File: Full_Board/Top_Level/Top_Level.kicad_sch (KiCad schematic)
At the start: 7 parts, among them J1 OQ0212500000G, J2 OQ0212500000G, J3 OQ0432500000G, J4 OQ0432500000G, J5 OQ0432500000G

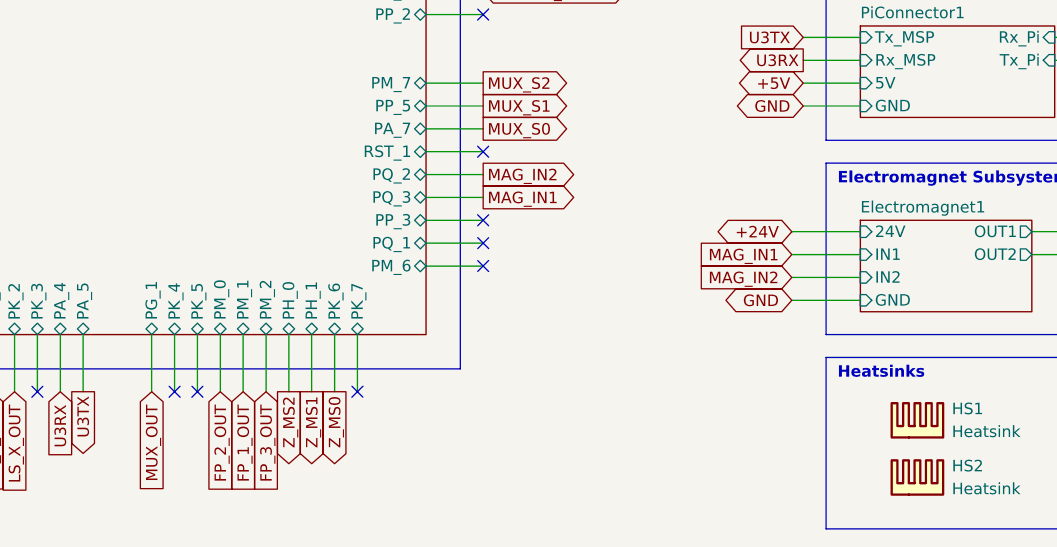
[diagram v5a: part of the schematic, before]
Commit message: Added traces for emag and increased the width of some power lines
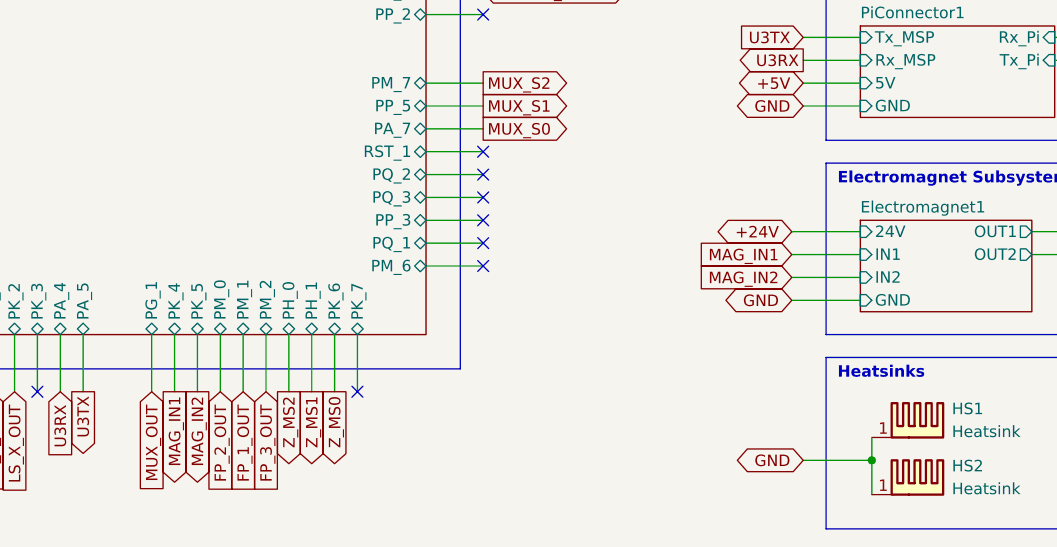
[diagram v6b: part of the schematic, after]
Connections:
- net GND: now also HS1.1, HS2.1
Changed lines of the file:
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@@
     (company "The Great Gambit")
   )
+  (junction (at 151.13 185.42) (diameter 0) (color 0 0 0 0)
+  )
   (no_connect (at 81.28 96.52))
   (no_connect (at 78.74 96.52))
@@
   (no_connect (at 40.64 96.52))
   (no_connect (at 107.95 135.89))
+  (no_connect (at 107.95 153.67))
+  (no_connect (at 107.95 156.21))
   (no_connect (at 107.95 158.75))
   (no_connect (at 107.95 120.65))
@@
   (no_connect (at 107.95 161.29))
   (no_connect (at 71.12 96.52))
-  (no_connect (at 73.66 177.8))
-  (no_connect (at 76.2 177.8))
   (no_connect (at 25.4 153.67))
   (no_connect (at 25.4 151.13))
@@
     (stroke (width 0) (type default) (color 0 0 0 0))
   )
+  (wire (pts (xy 101.6 153.67) (xy 107.95 153.67))
+    (stroke (width 0) (type default) (color 0 0 0 0))
+  )
   (wire (pts (xy 25.4 135.89) (xy 31.75 135.89))
     (stroke (width 0) (type default) (color 0 0 0 0))
   )
+  (wire (pts (xy 151.13 185.42) (xy 151.13 189.23))
+    (stroke (width 0) (type default) (color 0 0 0 0))
+  )
   (wire (pts (xy 101.6 151.13) (xy 107.95 151.13))
     (stroke (width 0) (type default) (color 0 0 0 0))
@@
     (stroke (width 0) (type default) (color 0 0 0 0))
   )
+  (wire (pts (xy 143.51 185.42) (xy 151.13 185.42))
+    (stroke (width 0) (type default) (color 0 0 0 0))
+  )
   (wire (pts (xy 223.52 36.83) (xy 228.6 36.83))
     (stroke (width 0) (type default) (color 0 0 0 0))
@@
     (stroke (width 0) (type default) (color 0 0 0 0))
   )
-  (polyline (pts (xy 226.06 154.94) (xy 226.06 119.38))
+  (wire (pts (xy 101.6 156.21) (xy 107.95 156.21))
     (stroke (width 0) (type default) (color 0 0 0 0))
   )
-  (wire (pts (xy 101.6 153.67) (xy 107.95 153.67))
+  (polyline (pts (xy 226.06 154.94) (xy 226.06 119.38))
     (stroke (width 0) (type default) (color 0 0 0 0))
   )
@@
     (stroke (width 0) (type default) (color 0 0 0 0))
   )
+  (wire (pts (xy 151.13 185.42) (xy 151.13 182.88))
+    (stroke (width 0) (type default) (color 0 0 0 0))
+  )
   (polyline (pts (xy 76.2 13.97) (xy 104.14 13.97))
     (stroke (width 0) (type default) (color 0 0 0 0))
@@
     (stroke (width 0) (type default) (color 0 0 0 0))
   )
-  (wire (pts (xy 101.6 156.21) (xy 107.95 156.21))
-    (stroke (width 0) (type default) (color 0 0 0 0))
-  )
   (wire (pts (xy 251.46 24.13) (xy 256.54 24.13))
     (stroke (width 0) (type default) (color 0 0 0 0))
@@
     )
   )
-  (global_label "MAG_IN2" (shape output) (at 107.95 153.67 0) (fields_autoplaced)
-    (effects (font (size 1.27 1.27)) (justify left))
-    (property "Intersheet References" "${INTERSHEET_REFS}" (id 0) (at 118.2855 153.7494 0)
-      (effects (font (size 1.27 1.27)) (justify left) hide)
+  (global_label "MAG_IN2" (shape output) (at 76.2 177.8 270) (fields_autoplaced)
+    (effects (font (size 1.27 1.27)) (justify right))
+    (property "Intersheet References" "${INTERSHEET_REFS}" (id 0) (at 76.1206 188.1355 90)
+      (effects (font (size 1.27 1.27)) (justify right) hide)
     )
   )
@@
     )
   )
-  (global_label "MAG_IN1" (shape output) (at 107.95 156.21 0) (fields_autoplaced)
-    (effects (font (size 1.27 1.27)) (justify left))
-    (property "Intersheet References" "${INTERSHEET_REFS}" (id 0) (at 118.2855 156.2894 0)
-      (effects (font (size 1.27 1.27)) (justify left) hide)
+  (global_label "MAG_IN1" (shape output) (at 73.66 177.8 270) (fields_autoplaced)
+    (effects (font (size 1.27 1.27)) (justify right))
+    (property "Intersheet References" "${INTERSHEET_REFS}" (id 0) (at 73.5806 188.1355 90)
+      (effects (font (size 1.27 1.27)) (justify right) hide)
     )
   )
@@
     )
   )
+  (global_label "GND" (shape bidirectional) (at 143.51 185.42 180) (fields_autoplaced)
+    (effects (font (size 1.27 1.27)) (justify right))
+    (property "Intersheet References" "${INTERSHEET_REFS}" (id 0) (at 137.2264 185.4994 0)
+      (effects (font (size 1.27 1.27)) (justify right) hide)
+    )
+  )
   (global_label "GND" (shape bidirectional) (at 143.51 146.05 180) (fields_autoplaced)
     (effects (font (size 1.27 1.27)) (justify right))
@@
       (effects (font (size 1.27 1.27)) hide)
     )
+    (pin "1")
   )
   (symbol (lib_id "OQ04325500000G:OQ0432500000G") (at 254 99.06 0) (unit 1)
@@
     (pin "2")
   )
-  (symbol (lib_id "Mechanical:Heatsink") (at 156.21 182.88 0) (unit 1)
+  (symbol (lib_name "Heatsink_1") (lib_id "Mechanical:Heatsink") (at 156.21 182.88 0) (unit 1)
     (in_bom yes) (on_board yes) (fields_autoplaced)
     (property "Reference" "HS1" (id 0) (at 160.02 179.7049 0)
@@
       (effects (font (size 1.27 1.27)) hide)
     )
+    (pin "1")
   )
   (symbol (lib_id "OQ04325500000G:OQ0432500000G") (at 254 67.31 0) (unit 1)
@@
       (reference "TP15") (unit 1) (value "~") (footprint "TestPoint:TestPoint_Keystone_5010-5014_Multipurpose")
     )
+    (path "/f059198e-ec55-48b1-bb71-d05bde55edab/63ce05dd-a994-434a-9d25-50da649a6ec3"
+      (reference "TP16") (unit 1) (value "~") (footprint "TestPoint:TestPoint_Keystone_5010-5014_Multipurpose")
+    )
+    (path "/f059198e-ec55-48b1-bb71-d05bde55edab/d8216112-e73b-4580-b202-27b92baacd12"
+      (reference "TP17") (unit 1) (value "~") (footprint "TestPoint:TestPoint_Keystone_5010-5014_Multipurpose")
+    )
     (path "/f355d1b6-bee3-4968-acb9-caad2ec6238b/51b51704-6420-43a3-8572-c2e2ef1291bf"

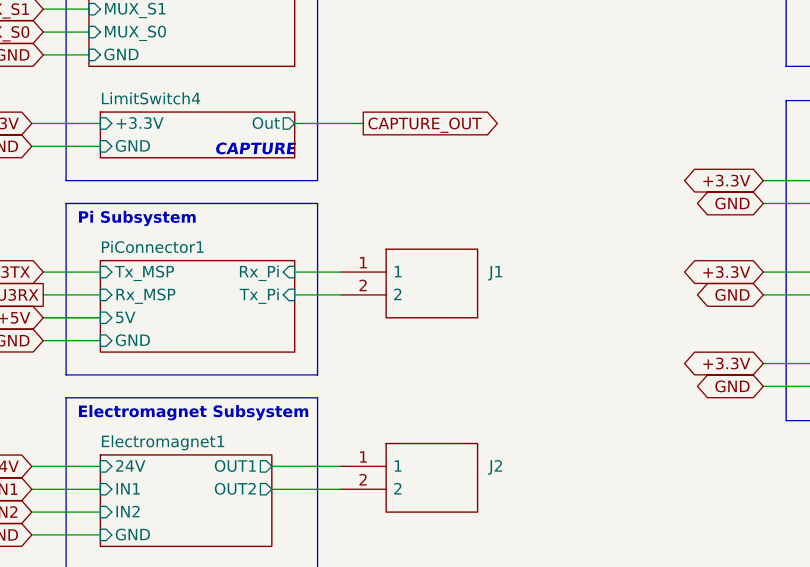
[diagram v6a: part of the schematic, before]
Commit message: Added Pi header
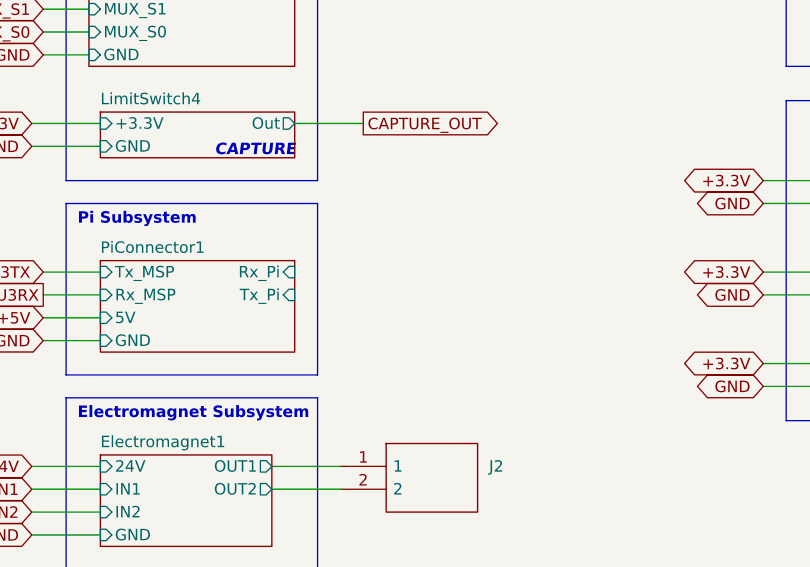
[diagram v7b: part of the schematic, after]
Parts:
- removed J1: OQ0212500000G, OQ0212500000G:OQ0212500000G, symbol OQ0212500000G:OQ0212500000G
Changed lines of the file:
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@@
     (stroke (width 0) (type default) (color 0 0 0 0))
   )
-  (wire (pts (xy 171.45 140.97) (xy 176.53 140.97))
-    (stroke (width 0) (type default) (color 0 0 0 0))
-  )
   (wire (pts (xy 86.36 171.45) (xy 86.36 177.8))
     (stroke (width 0) (type default) (color 0 0 0 0))
@@
     (stroke (width 0) (type default) (color 0 0 0 0))
   )
-  (wire (pts (xy 171.45 138.43) (xy 176.53 138.43))
-    (stroke (width 0) (type default) (color 0 0 0 0))
-  )
   (polyline (pts (xy 173.99 171.45) (xy 146.05 171.45))
     (stroke (width 0) (type default) (color 0 0 0 0))
@@
     (pin "2")
   )
-  (symbol (lib_id "OQ0212500000G:OQ0212500000G") (at 176.53 138.43 0) (unit 1)
-    (in_bom yes) (on_board yes) (fields_autoplaced)
-    (property "Reference" "J1" (id 0) (at 193.04 138.4299 0)
-      (effects (font (size 1.27 1.27)) (justify left))
-    )
-    (property "Value" "OQ0212500000G" (id 1) (at 193.04 140.9699 0)
-      (effects (font (size 1.27 1.27)) (justify left) hide)
-    )
-    (property "Footprint" "OQ0212500000G:OQ0212500000G" (id 2) (at 193.04 135.89 0)
-      (effects (font (size 1.27 1.27)) (justify left) hide)
-    )
-    (property "Datasheet" "https://datasheet.datasheetarchive.com/originals/distributors/DKDS-9/178262.pdf" (id 3) (at 193.04 138.43 0)
-      (effects (font (size 1.27 1.27)) (justify left) hide)
-    )
-    (property "Manufacturer_Part_Number" "OQ0212500000G" (id 4) (at 193.04 153.67 0)
-      (effects (font (size 1.27 1.27)) (justify left) hide)
-    )
-    (property "Digikey Part Number" "609-4981-ND" (id 5) (at 176.53 138.43 0)
-      (effects (font (size 1.27 1.27)) hide)
-    )
-    (property "Mouser Part Number" "649-220107-C021A01LF" (id 6) (at 193.04 146.05 0)
-      (effects (font (size 1.27 1.27)) (justify left) hide)
-    )
-    (property "Digikey Link" "https://www.digikey.com/en/products/detail/amphenol-anytek/OQ0212500000G/4242016" (id 7) (at 176.53 138.43 0)
-      (effects (font (size 1.27 1.27)) hide)
-    )
-    (property "Mouser Link" "" (id 8) (at 176.53 138.43 0)
-      (effects (font (size 1.27 1.27)) hide)
-    )
-    (property "Description" "Pluggable Terminal Blocks 2P 3.50MM HDR STR PLUGGABLE TERM BLK" (id 9) (at 193.04 140.97 0)
-      (effects (font (size 1.27 1.27)) (justify left) hide)
-    )
-    (property "Height" "9.2" (id 10) (at 193.04 143.51 0)
-      (effects (font (size 1.27 1.27)) (justify left) hide)
-    )
-    (property "Mouser Price/Stock" "https://www.mouser.co.uk/ProductDetail/Amphenol-Anytek/OQ0212500000G?qs=Mv7BduZupUhn3%2FKe8nJdbQ%3D%3D" (id 11) (at 193.04 148.59 0)
-      (effects (font (size 1.27 1.27)) (justify left) hide)
-    )
-    (property "Manufacturer_Name" "Amphenol" (id 12) (at 193.04 151.13 0)
-      (effects (font (size 1.27 1.27)) (justify left) hide)
-    )
-    (pin "1")
-    (pin "2")
-  )
   (symbol (lib_name "Heatsink_1") (lib_id "Mechanical:Heatsink") (at 156.21 182.88 0) (unit 1)
     (in_bom yes) (on_board yes) (fields_autoplaced)
@@
       (reference "IC5") (unit 1) (value "BD62130AEFJ-E2") (footprint "SOIC127P600X100-9N")
     )
-    (path "/c49c40d9-3b05-4cae-a1f5-15f0abbbf620"
-      (reference "J1") (unit 1) (value "OQ0212500000G") (footprint "OQ0212500000G:OQ0212500000G")
+    (path "/f355d1b6-bee3-4968-acb9-caad2ec6238b/508d28bd-e7f5-49bc-9c70-a4bbb093760b"
+      (reference "J1") (unit 1) (value "302-S101") (footprint "302-S101:302-S101")
     )
     (path "/eed9ac13-0553-4be8-a87c-cf15a0799b3e/e6ba01e7-fe50-4df3-8c33-307516bbd642"
@@
       (reference "JP20") (unit 1) (value "3.3V Jumper") (footprint "TestPoint:TestPoint_2Pads_Pitch2.54mm_Drill0.8mm")
     )
+    (path "/f355d1b6-bee3-4968-acb9-caad2ec6238b/eef6a18c-ca7e-4e66-8a10-57f0632619ae"
+      (reference "JP?") (unit 1) (value "5V Jumper") (footprint "TestPoint:TestPoint_2Pads_Pitch2.54mm_Drill0.8mm")
+    )
     (path "/0decb850-c73f-4a21-ac88-d022f064034a/8e575a13-eb08-41db-b5ab-de0d50d642ba"

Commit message: Clean DRC
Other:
- sheet PiConnector1 ports: added none; removed Rx_Pi, Tx_Pi
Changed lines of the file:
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@@
       (effects (font (size 1.27 1.27)) (justify left top) hide)
-    )
-    (pin "Rx_Pi" input (at 171.45 138.43 0)
-      (effects (font (size 1.27 1.27)) (justify right))
-    )
-    (pin "Tx_Pi" input (at 171.45 140.97 0)
-      (effects (font (size 1.27 1.27)) (justify right))
     )
     (pin "Tx_MSP" input (at 149.86 138.43 180)
@@
     )
     (path "/f355d1b6-bee3-4968-acb9-caad2ec6238b/eef6a18c-ca7e-4e66-8a10-57f0632619ae"
-      (reference "JP?") (unit 1) (value "5V Jumper") (footprint "TestPoint:TestPoint_2Pads_Pitch2.54mm_Drill0.8mm")
+      (reference "JP21") (unit 1) (value "5V Jumper") (footprint "TestPoint:TestPoint_2Pads_Pitch2.54mm_Drill0.8mm")
     )
     (path "/0decb850-c73f-4a21-ac88-d022f064034a/8e575a13-eb08-41db-b5ab-de0d50d642ba"
